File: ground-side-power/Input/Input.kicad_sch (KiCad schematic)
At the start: 36 parts, among them J1 Battery Terminals, J2 Battery Terminals, J26 Conn_01x02_Female, J3 Battery Terminals, J4 Battery Terminals, J5 874270842, J6 874270842, J7 ATX-24, J8 Conn_01x03_Female, J9 Conn_01x03_Female, K1 AZ2150-1A-12DEF, M1 Fan_PC_Chassis, SW1 GRB234A2NABA1, U1 INA180, U2 INA180

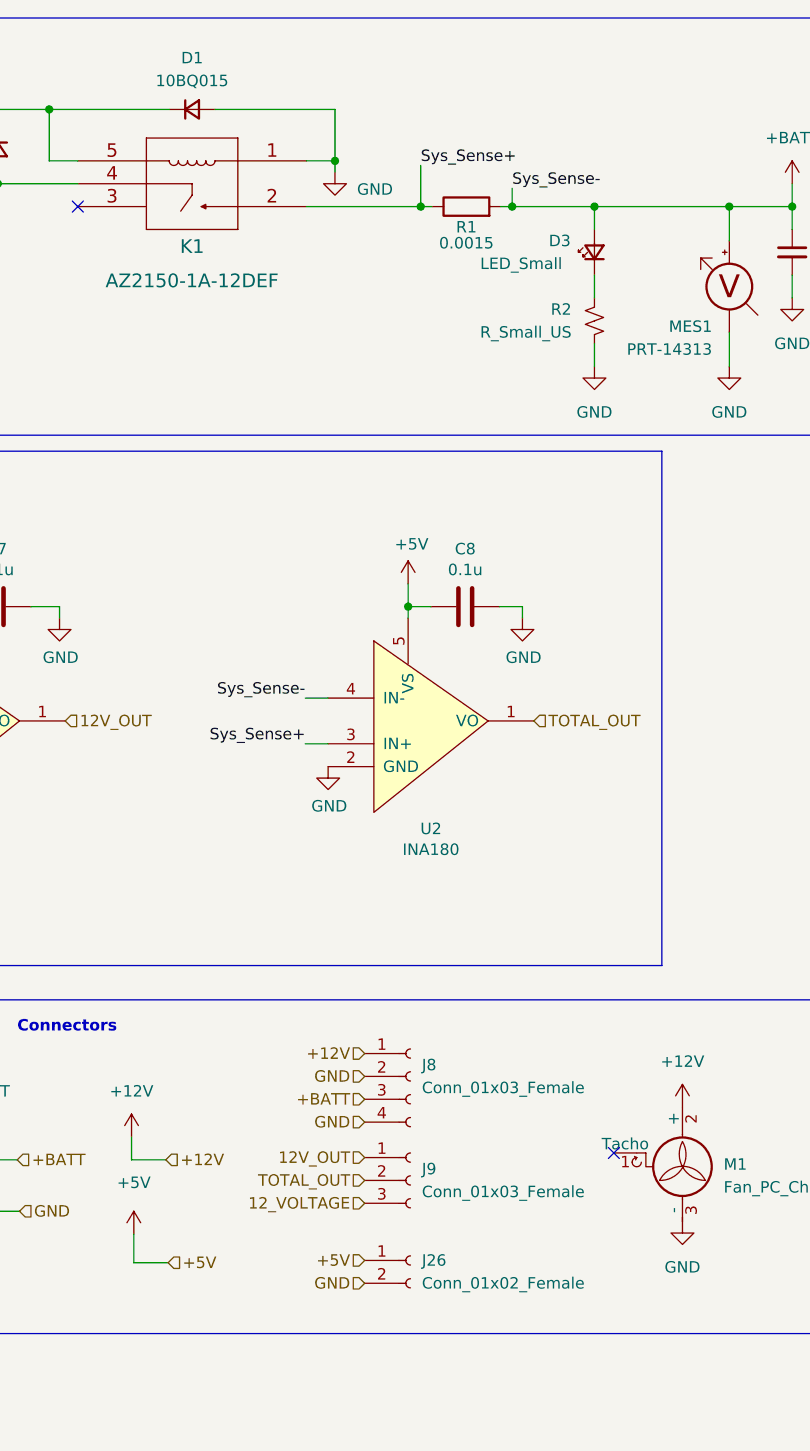
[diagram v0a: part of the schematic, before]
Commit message: resolved issues from testing
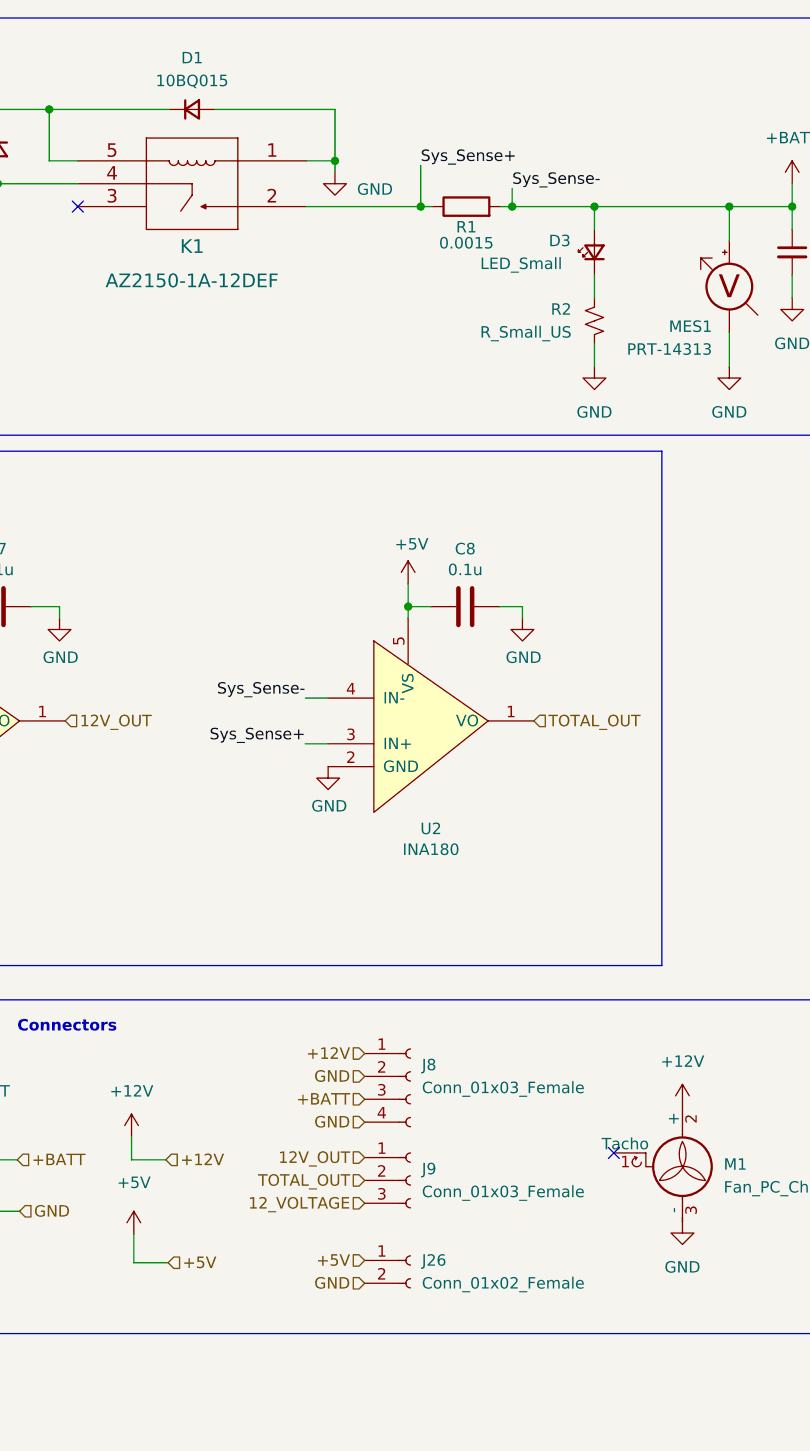
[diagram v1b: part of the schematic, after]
